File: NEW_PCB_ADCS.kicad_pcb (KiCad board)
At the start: 2 copper layers, 42 x 42 mm, 73 parts, among them IC1 DRV8212DSGR, IC2 DRV8212DSGR, IC3 DRV8212DSGR, J1 SWD, J2 PANEL1, J3 PANEL2, J4 PANEL3, J5 PANEL4, J6 MTQZ, J7 Micro_SD_Card_Det_Hirose_DM3AT, J8 PQ9-Connector, U1 AD8603, U2 47K, U3 STM32L476RGTx, U4 TCAN334, U5 LIS3MDL, U6 BNO055, Y1 Crystal

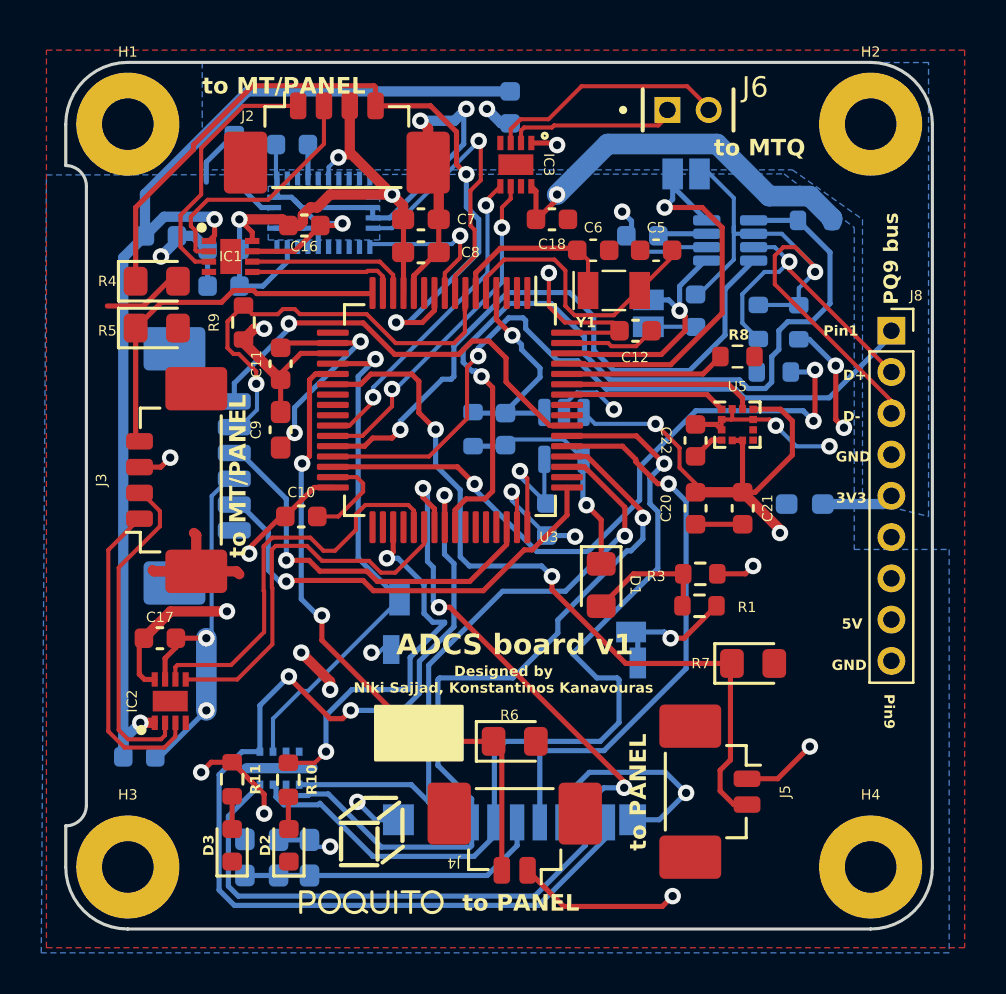
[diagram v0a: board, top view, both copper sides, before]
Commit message: Use pogo pins; move diode to back
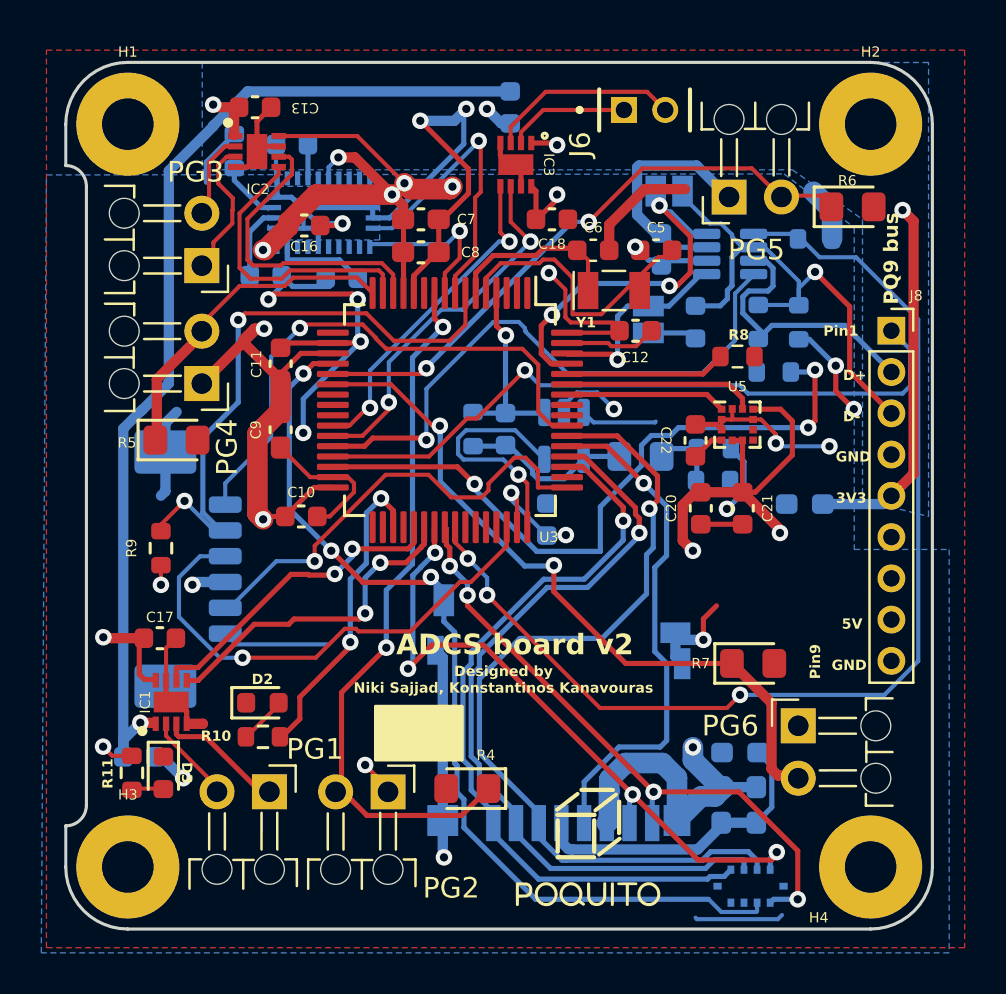
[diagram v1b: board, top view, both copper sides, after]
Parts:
- removed J2: PANEL1, Connector_Molex:Molex_PicoBlade_53398-0471_1x04-1MP_P1.25mm_Vertical
- removed J3: PANEL2, Connector_Molex:Molex_PicoBlade_53398-0471_1x04-1MP_P1.25mm_Vertical
- removed J4: PANEL3, Connector_Molex:Molex_PicoBlade_53398-0271_1x02-1MP_P1.25mm_Vertical
- removed J5: PANEL4, Connector_Molex:Molex_PicoBlade_53398-0271_1x02-1MP_P1.25mm_Vertical
- added PG1: Conn_01x02, lsf-kicad-lib:MillMax_8290-22-002-20-001101_1x02_P2.54mm_Horizontal, F.Cu at (183.1, 83.9)
- added PG2: Conn_01x02, lsf-kicad-lib:MillMax_8290-22-002-20-001101_1x02_P2.54mm_Horizontal, F.Cu at (188.8, 83.9)
- added PG3: Conn_01x02, lsf-kicad-lib:MillMax_8290-22-002-20-001101_1x02_P2.54mm_Horizontal, F.Cu at (179.8, 58.4)
- added PG4: Conn_01x02, lsf-kicad-lib:MillMax_8290-22-002-20-001101_1x02_P2.54mm_Horizontal, F.Cu at (179.8, 64.2)
- added PG5: Conn_01x02, lsf-kicad-lib:MillMax_8290-22-002-20-001101_1x02_P2.54mm_Horizontal, F.Cu at (205.3, 55.1)
- added PG6: Conn_01x02, lsf-kicad-lib:MillMax_8290-22-002-20-001101_1x02_P2.54mm_Horizontal, F.Cu at (208.7, 80.7)
- C13: moved to F.Cu
- D1, R1, R3: moved to B.Cu
- moved R6 30.6 mm to (211.3, 55.6)
- moved R4 28.8 mm to (192.6, 83.8), turned to 180 degrees
- moved IC2 27.0 mm to (182.5, 52.9), turned to 0 degrees
- moved L1 24.5 mm to (205.9, 82.0), turned to 0 degrees
- moved U2 23.5 mm to (206.4, 88.5), turned to 0 degrees
- moved C4 23.3 mm to (206.7, 84.6)
- moved IC1 21.8 mm to (178.3, 79.6), turned to 90 degrees
- moved C3 20.1 mm to (205.0, 84.6)
- moved G*** 16.3 mm to (185.8, 74.0), turned to -90 degrees
- moved R9 11.6 mm to (177.8, 72.1)
- moved G*** 10.5 mm to (198.5, 86.6)
- moved C13 7.72 mm to (182.4, 50.8)
- moved R3 7.65 mm to (204.6, 67.3)
- moved D2 7.03 mm to (182.7, 79.6), turned to 0 degrees
- moved D1 6.52 mm to (201.0, 67.7), turned to 0 degrees
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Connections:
- H1 pad 1: unconnected-(H1-Pad1) -> GND
- H2 pad 1: unconnected-(H2-Pad1) -> GND
- H3 pad 1: unconnected-(H3-Pad1) -> GND
- H4 pad 1: unconnected-(H4-Pad1) -> GND
- IC1 pad 9: unconnected-(IC1-EP-Pad9) -> GND
- IC2 pad 9: unconnected-(IC2-EP-Pad9) -> GND
- IC3 pad 9: unconnected-(IC3-EP-Pad9) -> GND
- J1 pad MP: (no net) -> VCCQ
- U3 pad 14: /MCU/MTQ1+ -> /MCU/MTQ2+
- U3 pad 15: /MCU/MTQ1- -> /MCU/MTQ2-
- U3 pad 37: /MCU/MTQ2+ -> /MCU/MTQ1+
- U3 pad 38: /MCU/MTQ2- -> /MCU/MTQ1-
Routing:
- net /Data Logging/D1: track 52.5 -> 30.6 mm, vias 3 -> 4
- net /Data Logging/SD_DET: track 25.1 -> 45.5 mm, vias 1 -> 3
- net /Data Logging/D0: track 49.2 -> 32.6 mm, vias 3 -> 4
- net /MCU/CAN1_EN: track 41.3 -> 54.2 mm, vias 1 -> 3
- net +3.3VP: track 59.8 -> 72.1 mm, vias 3 -> 4
- net /Connectors/MQT2+: track 15.8 -> 4.13 mm
- net /Connectors/MQT2-: track 15.4 -> 6.40 mm
- net /MCU/MTQ1-: track 7.27 -> 16.1 mm, vias 0 -> 2
- net /Connectors/MQT1+: track 12.2 -> 4.29 mm
- net /MCU/NRST: track 21.1 -> 28.8 mm, vias 1 -> 2
- net /MCU/MTQ1+: track 7.97 -> 15.6 mm, vias 0 -> 2
- net GND: track 140.6 -> 147.5 mm
- net /Connectors/MQT1-: track 12.4 -> 6.01 mm
- net /MCU/SWDIO: track 18.8 -> 24.6 mm
- net VCCQ: track 142.0 -> 147.5 mm, vias 21 -> 18
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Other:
- board text added: "ADCS board v2"
- board text removed: "ADCS board v1"
- board text removed: "to MT/PANEL"
- board text removed: "to MTQ"
- board text removed: "to PANEL"

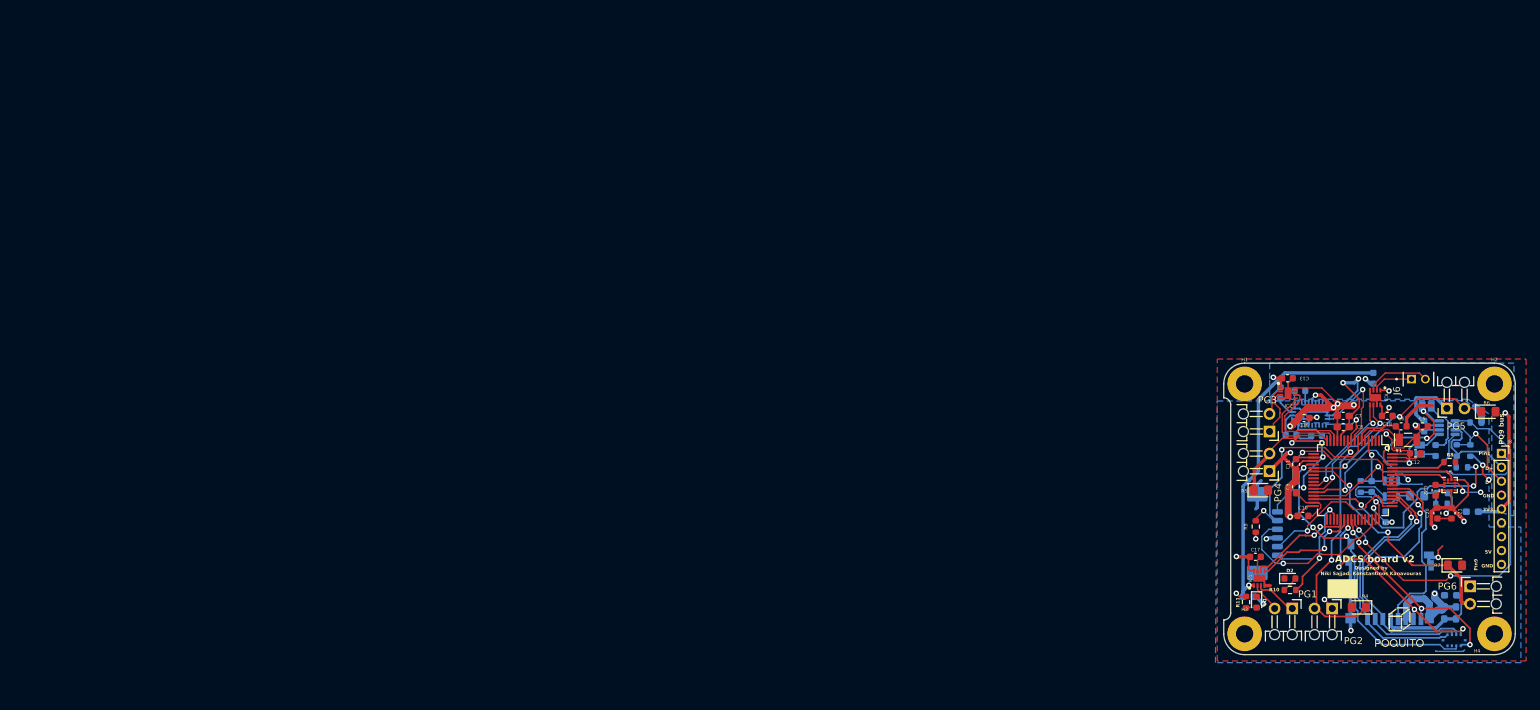
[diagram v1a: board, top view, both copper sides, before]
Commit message: Flip misaligned pogo pins
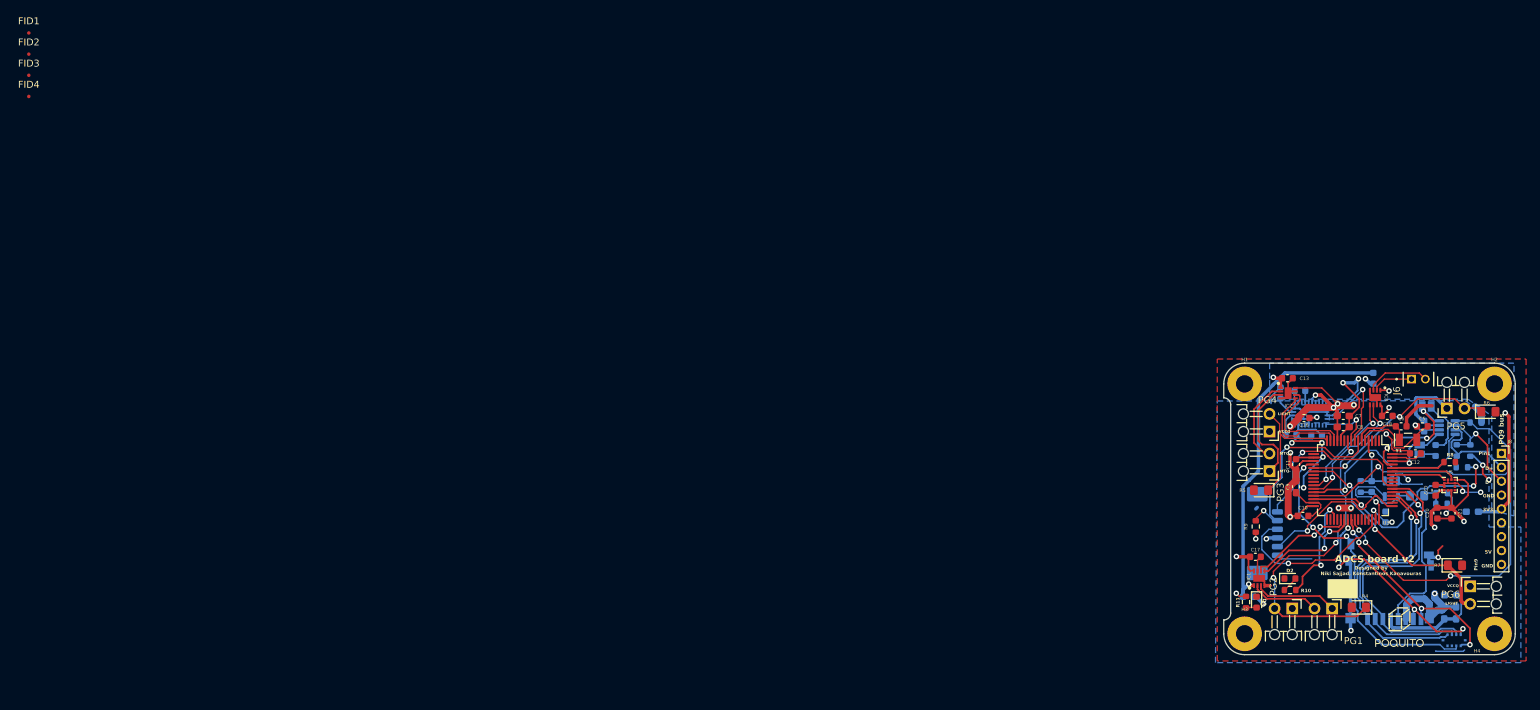
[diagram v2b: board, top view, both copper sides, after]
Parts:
- added FID1: Fiducial, Fiducial:Fiducial_0.5mm_Mask1.5mm, F.Cu at (1.02, 1.02)
- added FID2: Fiducial, Fiducial:Fiducial_0.5mm_Mask1.5mm, F.Cu at (1.02, 4.08)
- added FID3: Fiducial, Fiducial:Fiducial_0.5mm_Mask1.5mm, F.Cu at (1.02, 7.12)
- added FID4: Fiducial, Fiducial:Fiducial_0.5mm_Mask1.5mm, F.Cu at (1.02, 10.2)
- turned R5 to 180 degrees
- renumbered PG2 to PG1, PG1 to PG2, PG4 to PG3, PG3 to PG4
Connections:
- H1 pad 1: GND -> unconnected-(H1-Pad1)
- H2 pad 1: GND -> unconnected-(H2-Pad1)
- H3 pad 1: GND -> unconnected-(H3-Pad1)
- H4 pad 1: GND -> unconnected-(H4-Pad1)
- J1 pad MP: VCCQ -> (no net)
- PG1 pad 1: VCCQ -> /Connectors/MQT1-
- PG1 pad 2: /Connectors/LIGHT_1 -> /Connectors/MQT1+
- PG2 pad 1: /Connectors/MQT1- -> VCCQ
- PG2 pad 2: /Connectors/MQT1+ -> /Connectors/LIGHT_1
- PG3 pad 1: VCCQ -> /Connectors/MQT2-
- PG3 pad 2: /Connectors/LIGHT_2 -> /Connectors/MQT2+
- PG4 pad 1: /Connectors/MQT2- -> VCCQ
- PG4 pad 2: /Connectors/MQT2+ -> /Connectors/LIGHT_2
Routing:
- net /Connectors/LIGHT_1: track 34.5 -> 46.8 mm, vias 2 -> 3
- net /Connectors/MQT2-: track 6.40 -> 15.5 mm
- net VCCQ: track 147.5 -> 138.4 mm, vias 18 -> 19
- net /Connectors/MQT2+: track 4.13 -> 11.9 mm
- net /Connectors/MQT1-: track 6.01 -> 11.9 mm
- net /Connectors/MQT1+: track 4.29 -> 9.91 mm
- net /Connectors/LIGHT_2: track 16.1 -> 19.7 mm
- net /Data Logging/D2: track 35.9 -> 38.3 mm
- net /Data Logging/D3: track 37.0 -> 39.3 mm
- net /Data Logging/CMD: track 40.7 -> 42.2 mm
- net /MCU/LED: track 15.3 -> 16.1 mm
- net /Connectors/LIGHT_4: track 34.8 -> 34.1 mm
- net GND: track 147.5 -> 146.8 mm
- net /MCU/PB11|SDA|RX: track 33.4 -> 32.7 mm
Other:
- board text added: "LIGHT"
- board text added: "MTQ+"
- board text added: "MTQ-"
- board text added: "VCCQ"

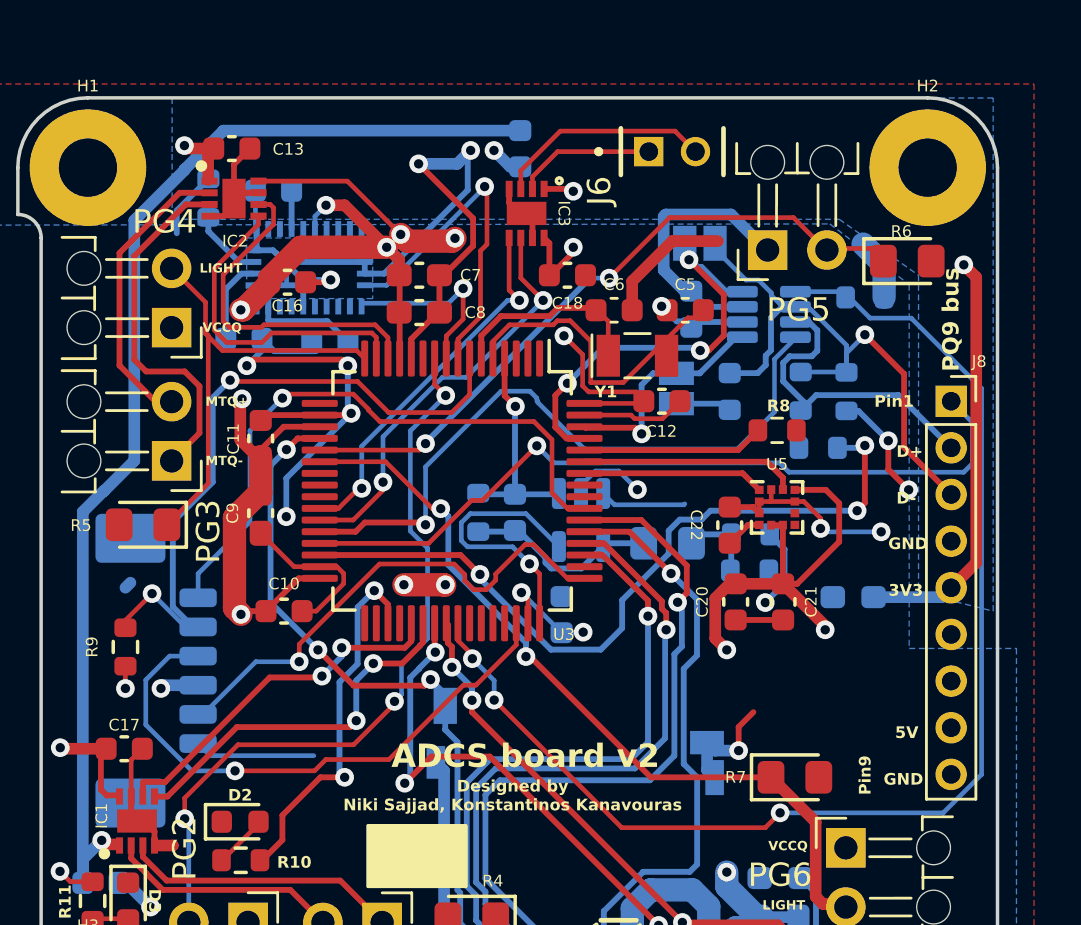
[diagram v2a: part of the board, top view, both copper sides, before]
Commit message: Update wrong MPNs
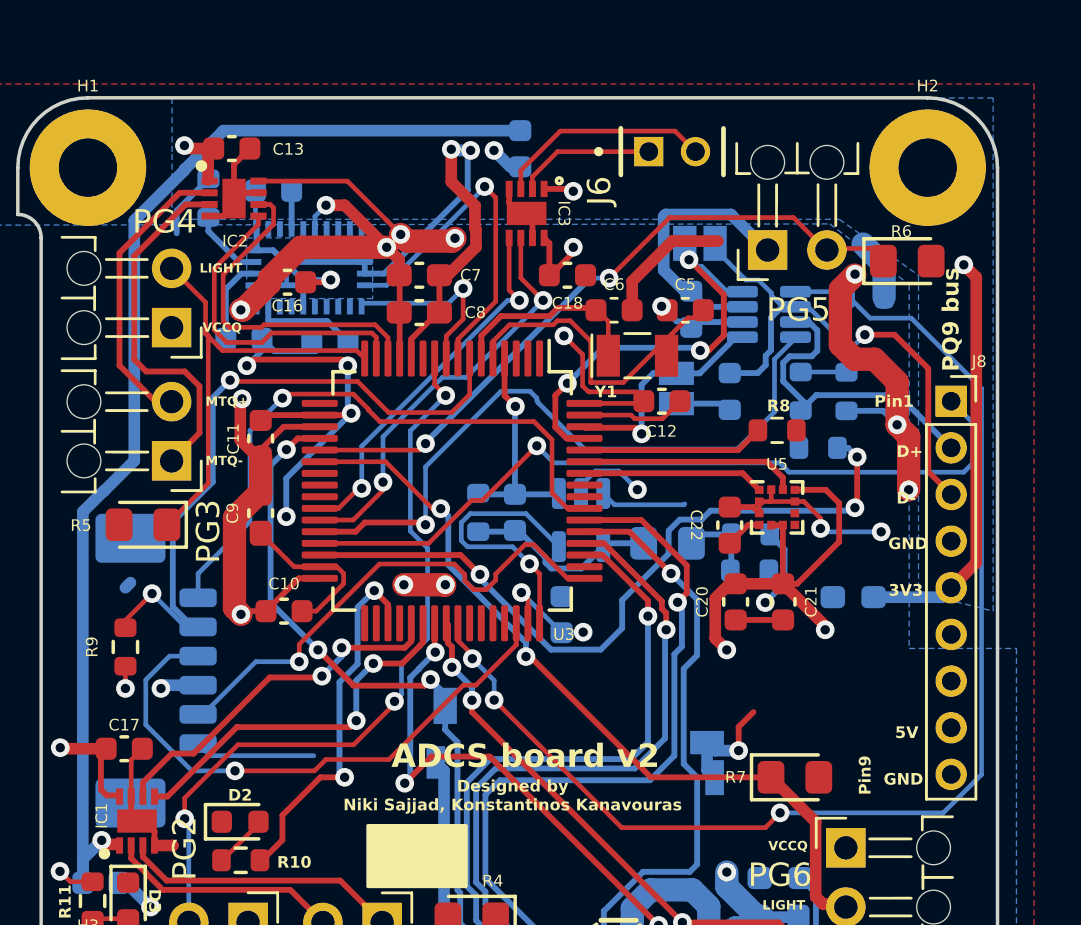
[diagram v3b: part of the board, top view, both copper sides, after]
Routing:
- net VCCQ: track 138.4 -> 147.2 mm, vias 19 -> 20
- net GND: track 146.8 -> 145.4 mm
- net /MCU/PB11|SDA|RX: track 32.7 -> 31.8 mm
- net /PQ Bus/D-: track 24.6 -> 25.3 mm

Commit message: Add ChipSat inhibit
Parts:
- added J2: MTQZ, Connector_JST:JST_SH_SM02B-SRSS-TB_1x02-1MP_P1.00mm_Horizontal, B.Cu at (208.8, 75.2)
- Y1: footprint Crystal:Crystal_SMD_MicroCrystal_CC7V-T1A-2Pin_3.2x1.5mm -> Crystal:Crystal_SMD_ECS_CSM3X-2Pin_7.6x4.1mm
- moved C5 7.55 mm to (208.0, 62.0), turned to 90 degrees
- moved C6 2.88 mm to (200.0, 55.1), turned to -90 degrees
- moved Y1 2.54 mm to (202.2, 58.9)
- moved C18 1.16 mm to (197.8, 55.7)
- moved C12 0.38 mm to (200.8, 62.0)
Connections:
- U3 pad 50: unconnected-(U3-PA15-Pad50) -> /Connectors/INHIBIT
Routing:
- net /Connectors/INHIBIT: track 0.00 -> 16.8 mm, vias 0 -> 1
- net GND: track 145.4 -> 137.0 mm, vias 20 -> 21
- net Net-(U3-PH0): track 13.4 -> 20.4 mm
- net VCCQ: track 147.2 -> 152.0 mm
- net /Connectors/LIGHT_3: track 29.1 -> 32.9 mm
- net Net-(U3-PH1): track 8.60 -> 11.0 mm
- net /Data Logging/D0: track 32.6 -> 31.5 mm
- net /MCU/CAN1RX: track 19.0 -> 18.0 mm
- net /PQ Bus/D-: track 25.3 -> 24.4 mm
- net /MCU/CAN1TX: track 9.57 -> 8.91 mm

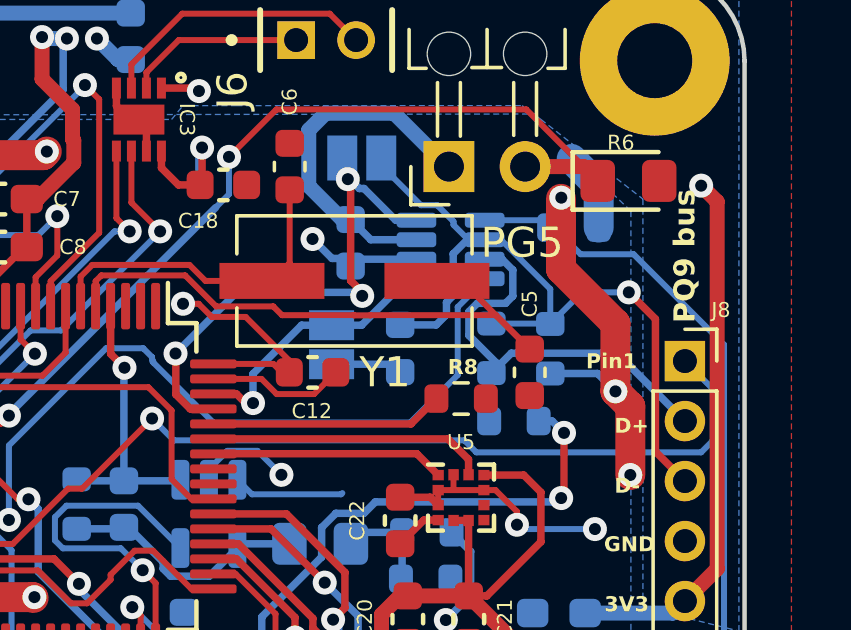
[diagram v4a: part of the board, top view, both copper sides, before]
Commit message: Add teardrops
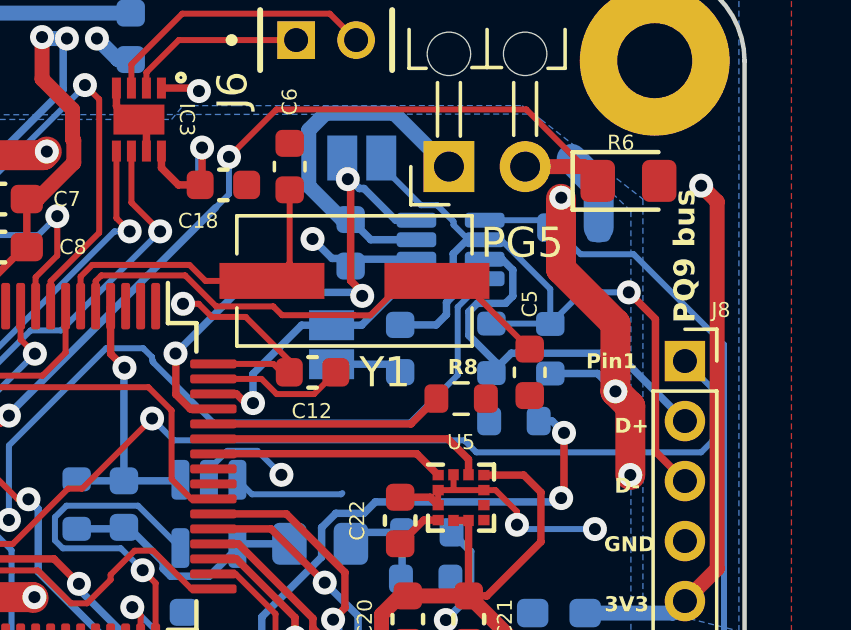
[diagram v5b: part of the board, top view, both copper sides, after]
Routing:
- net Net-(U3-PH0): track 20.4 -> 18.2 mm
